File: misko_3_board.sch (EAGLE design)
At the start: 151 parts, among them CN1 LiPo Battery, IC1 MC1525TT, IC2 FT230XS, IC3 LTC4425, IC4 FM25W256-SOIC, Q1 FDN304P, U1 ATMEGA1281-16AU, U2 SN74HCT14DR, U3 SN74LVC1G3157DBVR - BT switch, U4 SN74LVC1G3157DBVR - GPS switch, U5 TMP36GRTZ-REEL7, U6 TPS63030DSKT, U7 MCP73871-2AAI/ML, X1 MINI-USB_4P-32005-101, X3 FH12-24S-0.5SH

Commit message: 3-deck board consisting of : deck 1: lower side: power supply, upper side: cpu, spi bus, deck 2: lower side: sim800 + holder, upper side: bluetooth module, gps supercap+circuit deck3: lower side: misc, upper side: oled connector, gps, buttons, usb connector, led connectors, power switch
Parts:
- removed BOTTOM, TOP: FH12-24S-0.5SH, con-hirose:FH12-24S-0.5SH
- removed C10: 10µF, resistor:C-EUC0805
- removed C12: 4.7µF, resistor:C-EUC0805
- removed L3: 1.5µH, inductor-neosid:MS50
- removed L5: DJNR6045-100-S, DJNR6045-100S Power Inductor:DJNR6045-100-S
- removed R22: 150k, rcl:R-EU_R0805
- removed S2: GPRS push, switch-omron:10-XX
- removed S3: right, switch-omron:10-XX
- removed S4: left, switch-omron:10-XX
- removed SUPERCAP: 1F, capacitor-wima:C5/2.5
- removed SV1: (no value), con-lstb:MA05-2
- removed SV2: (no value), con-lstb:MA04-1
- removed U6: TPS63030DSKT, Texas Instruments_By_element14_Batch_1:TPS63030DSKT
- added B10: bottom, con-lstb:MA10-1
- added BL20: bottom left, con-lsta:FE20-1
- added BR20: bottom right, con-lsta:FE20-1
- added BT, VCC, VCC1, VCC5, V_GPS, V_LIION: PTR1TP14R, testpad:PTR1TP14R
- added C41: 0.1µF, rcl:C-EUC0805
- added C42: 4.7µF, rcl:C-EUC0805
- added DOWN: down, switch-omron:10-XX
- added GPS, SIM800, TP2: PTR1B1,27, testpad:PTR1B1,27
- added JP2: I2C, jumper:JP1E
- added M10: mid, con-lstb:MA10-1
- added ML20: mid left, con-lsta:FE20-1
- added MR20: mid right, con-lsta:FE20-1
- added R58: 46k, resistor:R-EU_R0805
- added R59: 150k, resistor:R-EU_R0805
- added RIGHT: right, switch-omron:10-XX
- added T10: top, con-lstb:MA10-1
- added TL20: top left, con-lsta:FE20-1
- added TP6: TPPAD1-17Y, testpad:TPPAD1-17Y
- added TR20: top right, con-lsta:FE20-1
- added U$10: DJNR3015-1R5, DJNR3015-1R5 Inductor:DJNR3015-1R5
- added U$8: 1F, EECRG0V105 SuperCap:1F
- added U$9: TPS63001DRCR, TI TPS63031:TPS63001DRCR
- added UP: up, switch-omron:10-XX
- ANT2: value (none) -> U.FL-R-SMT 1
- BT_LED, GPRS_LED, GPS_GREEN_LED, GPS_RED_LED: device led:LEDSML1206 -> led:LEDSQR2X5
- C1, C15, C3, C30: device resistor:C-EUC1206 -> resistor:C-EUC0805
- C18: value 100nF -> 10µF; device resistor:C-EUC1206 -> rcl:C-EUC0805
- R1, R15, R36, R37, R38, R39, R4, R40, R41, R5, R50, R51, R6, R7: device resistor:R-EU_R1206 -> resistor:R-EU_R0805
- R14, R42, R43, R44, R52, R53, R57: device resistor:R-EU_R1206 -> rcl:R-EU_M0805
- R48: value 1k -> 46k; device resistor:R-EU_R1206 -> resistor:R-EU_R0805
- S1: value up -> left
- S6: value down -> GPRS
- SJ1: value (none) -> GPIO6
- SJ2: value (none) -> RESET
- USB_RX_LED, USB_TX_LED: device led:LEDSML1206 -> led:LEDCHIPLED_1206
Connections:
- net N$11 renamed VPCC
- net N$18 renamed THERM
- net N$22 renamed PROG1
- net N$23 renamed PROG3
- net N$24 renamed PFI
- net N$25 renamed LTC4425_PROG
- net N$26 renamed LTC4425_EN
- net N$27 renamed PFI_RET
- net N$32 renamed VMID
- net N$33 renamed GPIO7
- net N$36 renamed GPIO4
- net N$38 renamed GPIO6
- net N$40 renamed ADXL345SDA
- net N$46 renamed GSM_ANT
- net N$7 renamed USBDP
- net N$9 renamed USBDM
- net VBAT+ renamed V_LIION+
- removed net N$100: BOTTOM-23.1
- removed net N$12: IC2.RXD, R3.2
- removed net N$13: R1.2
- removed net N$15: U7.*TE, U7.CE, U7.PROG2, U7.SEL
- removed net N$3: IC2.TXD, R2.2
- removed net N$34: BT_LED.A, C6.2, Q1.D, U$3.VCC
- removed net N$44: GPRS_LED.A, R50.2
- removed net N$45: R50.1, U$1.NETLIGHT
- removed net N$47: U$1.GND10, U$1.GND9
- removed net N$48: U$1.GND6, U$1.GND7
- removed net N$5: L5.1, SV2.4
- removed net N$53: L3.2, U6.L1
- removed net N$54: L3.1, U6.L2
- removed net N$8: R5.1, USB_TX_LED.A
- removed net N$86: BOTTOM-21.1
- removed net N$87: BOTTOM-22.1
- removed net N$90: TOP-23.1
- removed net N$91: TOP-22.1
- removed net N$92: TOP-21.1
- removed net S1: C2.2, R8.2, U2.1A
- removed net S2: C4.2, R10.2, U2.2A
- removed net S3: C5.2, R12.2, U2.3A
- removed net S4: C7.2, R18.2, U2.4A
- removed net S5: C8.2, R17.2, U2.5A
- removed net S6: C9.2, R16.2, U2.6A
- removed net VBAT: C11.1, C12.2, C26.2, R51.2, S8.2, U$1.VBAT1, U$1.VBAT2, U$1.VRTC, U6.PS/SYNC, U6.VIN, U6.VINA, U7.OUT, U7.OUT_2
- new net BLUETOOTH: BR20.15, C8.2, MR20.15, R17.2, TR20.15, U2.5A
- new net BLUE_LED: BL20.14, BT_LED.A, C6.2, ML20.14, Q1.D, TL20.14, U$3.VCC
- new net DOWN: BR20.12, C4.2, MR20.12, R10.2, TR20.12, U2.2A
- new net EN: BL20.20, ML20.20, R59.2, S8.1, TL20.20, U$9.EN
- new net GPRS: BR20.16, C9.2, MR20.16, R16.2, TR20.16, U2.4A
- new net GPRS_LED: BR20.18, GPRS_LED.A, MR20.18, TR20.18, U$1.NETLIGHT
- new net GPS_ON_OFF: BL20.11, GPS.TP, ML20.11, R1.1, R36.1, TL20.11, TP2.TP, U$2.ON_OFF
- new net L1: U$10.L1, U$9.L1
- new net L2: U$10.L2, U$9.L2
- new net LEFT: BR20.11, C2.2, MR20.11, R8.2, TR20.11, U2.1A
- new net N$33: GPRS_LED.C, R50.1
- new net PA7: BL20.15, ML20.15, TL20.15, U1.PA7_(AD7)
- new net PD7: U1.(T0)_PD7
- new net PE2: B10.7, M10.7, T10.7, U1.(XCK0/AIN0)_PE2
- new net PE3: B10.6, M10.6, T10.6, U1.(OC3A/AIN1)_PE3
- new net PE7: U1.(ICP3/CLKO/INT7)_PE7
- new net PG0: U1.PG0_(~WR)
- new net PG1: U1.PG1_(~RD)
- new net PG2: BL20.16, ML20.16, TL20.16, U1.PG2_(ALE)
- new net RIGHT: BR20.14, C7.2, MR20.14, R18.2, TR20.14, U2.6A
- new net RXD: BL20.1, IC2.RXD, ML20.1, R3.2, TL20.1
- new net TXD: BL20.2, IC2.TXD, ML20.2, R2.2, TL20.2
- new net UP: BR20.13, C5.2, MR20.13, R12.2, TR20.13, U2.3A
- new net V_LIION_REGULATED: BL20.19, C11.1, C26.2, C42.2, ML20.19, R51.2, S8.2, TL20.19, U$1.VBAT1, U$1.VBAT2, U$1.VRTC, U$9.PS/SYNC, U$9.VIN, U$9.VINA, U7.OUT, U7.OUT_2, V_LIION.TP
- new net V_SUPERCAP_SENSE_PIN: R48.2, R58.1, U1.PF2_(ADC2)
- net 5V0: now also BR20.20, MR20.20, TR20.20, U7.*TE, U7.CE, U7.PROG2, U7.SEL; no longer C18.2, L5.2
- net ADXL345_INT1_INTERRUPT_PIN: now also U1.(T3/INT6)_PE6; no longer U1.(ICP3/CLKO/INT7)_PE7
- net ANALOG_SW_CTRL_PIN: now also BR20.1, MR20.1, TR20.1, U1.(OC1B/PCINT6)_PB6, VCC1.TP; no longer BOTTOM-13.1, TOP-13.1, U1.(TOSC2)_PG3
- net ANTENNA: now also ANT2.ANT; no longer ANT2.1
- net BAT_A_PIN: now also U1.PF3_(ADC3); no longer U1.PF2_(ADC2)
- net BLUETOOTH_WAKEUP_PIN: now also BL20.13, BT.TP, ML20.13, TL20.13, U1.PA3_(AD3); no longer U1.(OC0A/OC1C/PCINT7)_PB7
- net GND: now also ANT2.GND1, ANT2.GND2, B10.9, BL20.5, BR20.5, C41.2, C42.1, DOWN.P, DOWN.P1, M10.9, ML20.5, MR20.5, R50.2, R58.2, R59.1, RIGHT.P, RIGHT.P1, T10.9, TL20.5, TP6.TP, TR20.5, U$1.GND10, U$1.GND6, U$1.GND7, U$1.GND9, U$7.GND6, U$7.GND7, U$8.+, U$9.GND, U$9.PGND, UP.P, UP.P1; no longer BOTTOM-1.1, BOTTOM-24.1, C10.1, C12.1, GPRS_LED.C, R22.2, S2.P, S2.P1, S3.P, S3.P1, S4.P, S4.P1, SUPERCAP.1, SV1.10, SV1.2, SV2.1, TOP-1.1, TOP-24.1, U6.GND, U6.PGND
- net GPS_GREEN_LED_PIN: now also BL20.17, ML20.17, TL20.17; no longer BOTTOM-10.1, BOTTOM-12.1, TOP-10.1, TOP-12.1
- net GPS_POWER_CTL_PIN: now also R1.2, U1.PA2_(AD2); no longer BOTTOM-18.1, R1.1, R36.1, TOP-18.1, U$2.ON_OFF, U1.(T0)_PD7
- net GPS_RED_LED_PIN: now also BL20.18, ML20.18, TL20.18; no longer BOTTOM-11.1, BOTTOM-9.1, TOP-11.1, TOP-9.1
- net GPS_SW_SERIAL_RX: now also B10.2, M10.2, T10.2; no longer BOTTOM-19.1, TOP-19.1
- net GPS_SW_SERIAL_TX: now also B10.1, M10.1, T10.1; no longer BOTTOM-20.1, TOP-20.1
- net GPS_TX: now also BL20.12, ML20.12, TL20.12
- net GPS_WAKEUP_PIN: now also BL20.10, ML20.10, TL20.10, U1.PA1_(AD1); no longer BOTTOM-17.1, TOP-17.1, U1.(TOSC1)_PG4
- net I2C_SCL_PIN: now also JP2.1; no longer SV2.3
- net I2C_SDA_PIN: now also JP2.2; no longer SV2.2
- net JTAG_TCL_PIN: now also BL20.6, ML20.6, TL20.6; no longer SV1.1
- net JTAG_TDI_PIN: now also BL20.9, ML20.9, TL20.9; no longer SV1.9
- net JTAG_TDO_PIN: now also BL20.8, ML20.8, TL20.8; no longer SV1.3
- net JTAG_TMS_PIN: now also BL20.7, ML20.7, TL20.7; no longer SV1.5
- net MCP73871_CHARGE_STATUS_1_PIN: now also U1.PA4_(AD4); no longer U1.PA2_(AD2)
- net MCP73871_CHARGE_STATUS_2_PIN: now also U1.PA5_(AD5); no longer U1.PA1_(AD1)
- net MCP73871_POWER_GOOD_PIN: now also U1.PA6_(AD6); no longer U1.PA0_(AD0)
- net MENU_BLUETOOTH_POWER_TOGGLE_PIN: now also U1.PC4_(A12); no longer BOTTOM-4.1, TOP-4.1, U1.PC1_(A9)
- net MENU_DOWN_BUTTON_PIN: now also U1.PC1_(A9), U2.2Y; no longer BOTTOM-5.1, TOP-5.1, U1.PC2_(A10), U2.6Y
- net MENU_GPRS_PUSH_BUTTON_PIN: now also U1.PC5_(A13), U2.4Y; no longer BOTTOM-7.1, TOP-7.1, U1.PC4_(A12), U2.2Y
- net MENU_LEFT_BUTTON_PIN: now also U2.1Y; no longer BOTTOM-3.1, TOP-3.1, U2.4Y
- net MENU_RIGHT_BUTTON_PIN: now also U1.PC3_(A11), U2.6Y; no longer BOTTOM-8.1, TOP-8.1, U1.PC5_(A13), U2.3Y
- net MENU_UP_BUTTON_PIN: now also U1.PC2_(A10), U2.3Y; no longer BOTTOM-6.1, TOP-6.1, U1.PC3_(A11), U2.1Y
- net N$1: now also R5.2, USB_TX_LED.A; no longer R22.1, S8.1, U6.EN
- net N$16: now also UP.S, UP.S1; no longer S3.S, S3.S1
- net N$21: now also DOWN.S, DOWN.S1; no longer S2.S, S2.S1
- net N$30: now also RIGHT.S, RIGHT.S1; no longer S4.S, S4.S1
- net PDI_UART0_CTS_PIN: now also BL20.3, ML20.3, TL20.3; no longer BOTTOM-16.1, TOP-16.1
- net PDI_UART0_RX_PIN: no longer BOTTOM-14.1, TOP-14.1
- net PDI_UART0_TX_PIN: no longer BOTTOM-15.1, TOP-15.1
- net RESET: now also BR20.17, MR20.17, TR20.17; no longer SV1.6
- net SD_CARD_DETECT_PIN: no longer U1.(OC1B/PCINT6)_PB6
- net SIM800C_CTS_PIN: now also BR20.8, MR20.8, TR20.8
- net SIM800C_POWER_PIN: now also BR20.10, MR20.10, SIM800.TP, TR20.10; no longer R48.1, U$1.VDD_EXT
- net SIM800C_RX_PIN: now also BR20.6, MR20.6, TR20.6
- net SIM800C_STATUS_PIN: now also BR20.9, MR20.9, TR20.9
- net SIM800C_TX_PIN: now also BR20.7, MR20.7, TR20.7
- net SIM_DETECT: no longer R48.2
- net SPI_FRAM_SS_PIN: now also U1.(OC3B/INT4)_PE4; no longer U1.(~SS/PCINT0)_PB0
- net SPI_MISO_PIN: now also B10.3, M10.3, T10.3
- net SPI_MOSI_PIN: now also B10.4, M10.4, T10.4
- net SPI_OLED_D/C_PIN: now also BR20.3, MR20.3, TR20.3, U1.(TOSC2)_PG3; no longer U1.(OC3B/INT4)_PE4
- net SPI_OLED_RESET_PIN: now also BR20.2, MR20.2, TR20.2, U1.(OC0A/OC1C/PCINT7)_PB7; no longer U1.(OC3A/AIN1)_PE3
- net SPI_SCK_PIN: now also B10.5, M10.5, T10.5
- net SPI_SS_ADXL345_PIN: now also U1.(OC3C/INT5)_PE5; no longer U1.(XCK0/AIN0)_PE2
- net SPI_SS_OLED_PIN: now also BR20.4, MR20.4, TR20.4, U1.(TOSC1)_PG4; no longer U1.(OC3C/INT5)_PE5
- net SPI_SS_SD_CARD_PIN: now also U1.(~SS/PCINT0)_PB0; no longer U1.(T3/INT6)_PE6
- net TMP36_SHUTDOWN_PIN: now also U1.PA0_(AD0); no longer U1.PA3_(AD3)
- net VCC: now also BL20.4, BR20.19, C18.2, C41.1, ML20.4, MR20.19, TL20.4, TR20.19, U$7.VCC, U$9.FB, U$9.VOUT, VCC.TP, VCC5.TP; no longer BOTTOM-2.1, C10.2, SV1.4, TOP-2.1, U6.FB, U6.VOUT
- net VGPS: now also B10.8, M10.8, R48.1, T10.8, U$8.-, V_GPS.TP; no longer SUPERCAP.2
- net VUSB: now also R5.1; no longer R5.2
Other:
- note added: "VUSB (aka. supercap voltage) measurement"
- note removed: "I2C Connector"
- note removed: "JTAG Header"
- moved on the sheet: BT_LED, C18, C28, C29, GPRS_LED, GPS_GREEN_LED, GPS_RED_LED, L2, R36, R4, R41, R45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

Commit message: - further progress on the 3-deck board, top portion needs rework due to final oled module
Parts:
- removed C30: 100nF, resistor:C-EUC0805
- removed DOWN: down, switch-omron:10-XX
- removed L1: DJNR6045-100-S, DJNR6045-100S Power Inductor:DJNR6045-100-S
- removed RIGHT: right, switch-omron:10-XX
- removed S1: left, switch-omron:10-XX
- removed S5: Bluetooth, switch-omron:10-XX
- removed S6: GPRS, switch-omron:10-XX
- removed UP: up, switch-omron:10-XX
- removed X1: MINI-USB_4P-32005-101, con-cypressindustries:MINI-USB_4P-32005-101
- added BLUETOOTH: BT, switch-omron:10-XX
- added C10: 100nF, resistor:C-EUC0805
- added GPRS: gprs, switch-omron:10-XX
- added L3: DJNR6045-100-S, DJNR6045-100S Power Inductor:DJNR6045-100-S
- added U$11: MX500075-1517USB_MINI-B, MX500075-1517 USB Mini-B straight socket:MX500075-1517USB_MINI-B
- added U$12: MICROJOYSTICK, micro joystick:MICROJOYSTICK
- U$8: value 1F -> EECS5R5H155; device EECRG0V105 SuperCap:1F -> EECS5R5H155 Supercap:EECS5R5H155
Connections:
- removed net N$14: R8.1, R9.1, S1.S, S1.S1
- removed net N$16: R12.1, R13.1, UP.S, UP.S1
- removed net N$21: DOWN.S, DOWN.S1, R10.1, R11.1
- removed net N$28: R17.1, R20.1, S5.S, S5.S1
- removed net N$29: R16.1, R19.1, S6.S, S6.S1
- removed net N$30: R18.1, R21.1, RIGHT.S, RIGHT.S1
- new net BUTTON_BLUETOOTH: BLUETOOTH.S, BLUETOOTH.S1, R17.1, R20.1
- new net BUTTON_CENTER: U$12.CENTER
- new net BUTTON_DOWN: R10.1, R11.1, U$12.DOWN
- new net BUTTON_GPRS: GPRS.S, GPRS.S1, R16.1, R19.1
- new net BUTTON_LEFT: R8.1, R9.1, U$12.LEFT
- new net BUTTON_RIGHT: R18.1, R21.1, U$12.RIGHT
- new net BUTTON_UP: R12.1, R13.1, U$12.UP
- net 5V0: now also C10.2, L3.2; no longer C30.2, L1.1
- net GND: now also BLUETOOTH.P, BLUETOOTH.P1, C10.1, GPRS.P, GPRS.P1, U$11.GND, U$12.GND1; no longer C30.1, DOWN.P, DOWN.P1, RIGHT.P, RIGHT.P1, S1.P, S1.P1, S5.P, S5.P1, S6.P, S6.P1, UP.P, UP.P1, X1.4
- net USB_D+: now also U$11.DP; no longer X1.3
- net USB_D-: now also U$11.DN; no longer X1.2
- net VUSB: now also L3.1, U$11.VBUS; no longer L1.2, X1.1

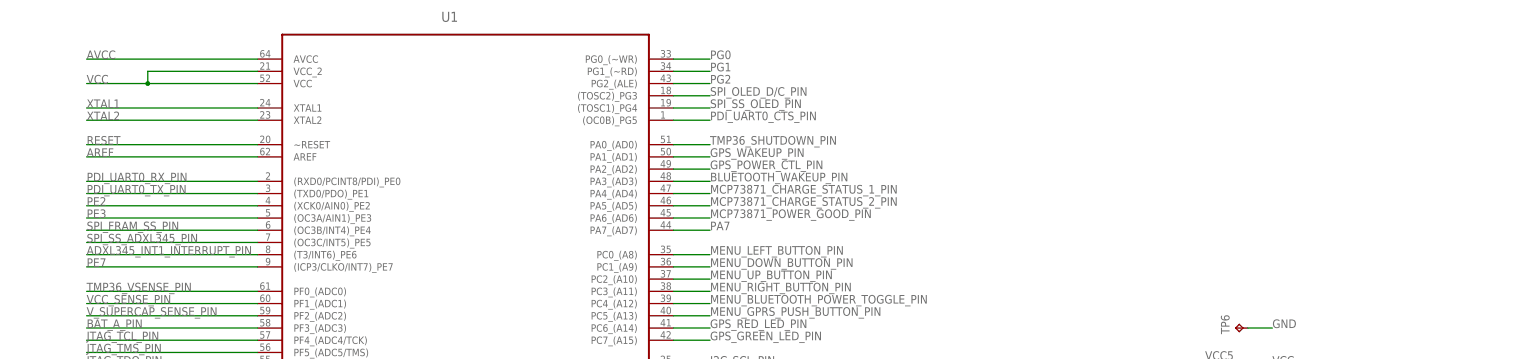
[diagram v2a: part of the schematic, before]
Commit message: - correction of int7 pin (-> adxl345 int1)
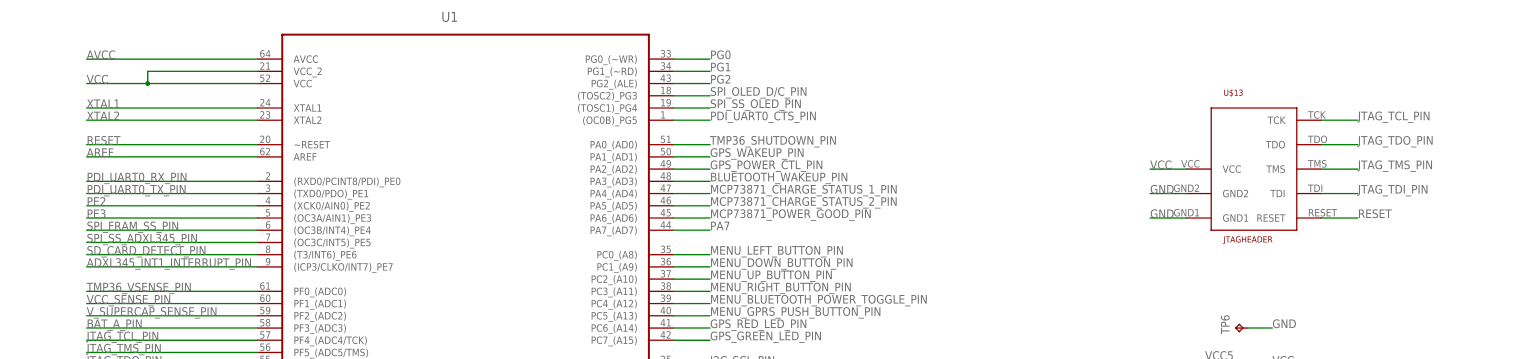
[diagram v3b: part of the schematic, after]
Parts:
- added U$13: JTAGHEADER, DS1031-14 - IDC socket:JTAGHEADER
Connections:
- removed net PE7: U1.(ICP3/CLKO/INT7)_PE7
- net ADXL345_INT1_INTERRUPT_PIN: now also U1.(ICP3/CLKO/INT7)_PE7; no longer U1.(T3/INT6)_PE6
- net GND: now also U$13.GND1, U$13.GND2
- net JTAG_TCL_PIN: now also U$13.TCK
- net JTAG_TDI_PIN: now also U$13.TDI
- net JTAG_TDO_PIN: now also U$13.TDO
- net JTAG_TMS_PIN: now also U$13.TMS
- net RESET: now also U$13.RESET
- net SD_CARD_DETECT_PIN: now also U1.(T3/INT6)_PE6
- net VCC: now also U$13.VCC
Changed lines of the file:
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@@
 <part name="BLUETOOTH" library="switch-omron" deviceset="10-XX" device="" value="BT"/>
 <part name="GPRS" library="switch-omron" deviceset="10-XX" device="" value="gprs"/>
+<part name="U$13" library="DS1031-14 - IDC socket" deviceset="JTAGHEADER" device=""/>
 </parts>
 <sheets>
@@
 <instance part="BLUETOOTH" gate="1" x="20.32" y="388.62" rot="R270"/>
 <instance part="GPRS" gate="1" x="20.32" y="363.22" rot="R270"/>
+<instance part="U$13" gate="G$1" x="294.64" y="802.64"/>
 </instances>
 <busses>
@@
 <label x="279.4" y="759.46" size="1.778" layer="95"/>
 </segment>
+<segment>
+<pinref part="U$13" gate="G$1" pin="VCC"/>
+<wire x1="261.62" y1="800.1" x2="254" y2="800.1" width="0.1524" layer="91"/>
+<label x="254" y="800.1" size="1.778" layer="95"/>
+</segment>
 </net>
 <net name="GND" class="0">
@@
 <label x="208.28" y="342.9" size="1.778" layer="95"/>
 </segment>
+<segment>
+<pinref part="U$13" gate="G$1" pin="GND1"/>
+<wire x1="261.62" y1="789.94" x2="254" y2="789.94" width="0.1524" layer="91"/>
+<label x="254" y="789.94" size="1.778" layer="95"/>
+</segment>
+<segment>
+<pinref part="U$13" gate="G$1" pin="GND2"/>
+<wire x1="261.62" y1="795.02" x2="254" y2="795.02" width="0.1524" layer="91"/>
+<label x="254" y="795.02" size="1.778" layer="95"/>
+</segment>
 </net>
 <net name="5V0" class="1">
@@
 <label x="523.24" y="782.32" size="1.778" layer="95"/>
 </segment>
+<segment>
+<pinref part="U$13" gate="G$1" pin="TDI"/>
+<wire x1="289.56" y1="795.02" x2="297.18" y2="795.02" width="0.1524" layer="91"/>
+<label x="297.18" y="795.02" size="1.778" layer="95"/>
+</segment>
 </net>
 <net name="JTAG_TDO_PIN" class="2">
@@
 <label x="523.24" y="779.78" size="1.778" layer="95"/>
 </segment>
+<segment>
+<pinref part="U$13" gate="G$1" pin="TDO"/>
+<wire x1="289.56" y1="805.18" x2="297.18" y2="805.18" width="0.1524" layer="91"/>
+<label x="297.18" y="805.18" size="1.778" layer="95"/>
+</segment>
 </net>
 <net name="JTAG_TMS_PIN" class="2">
@@
 <label x="523.24" y="777.24" size="1.778" layer="95"/>
 </segment>
+<segment>
+<pinref part="U$13" gate="G$1" pin="TMS"/>
+<wire x1="289.56" y1="800.1" x2="297.18" y2="800.1" width="0.1524" layer="91"/>
+<label x="297.18" y="800.1" size="1.778" layer="95"/>
+</segment>
 </net>
 <net name="JTAG_TCL_PIN" class="2">
@@
 <label x="523.24" y="774.7" size="1.778" layer="95"/>
 </segment>
+<segment>
+<pinref part="U$13" gate="G$1" pin="TCK"/>
+<wire x1="289.56" y1="810.26" x2="297.18" y2="810.26" width="0.1524" layer="91"/>
+<label x="297.18" y="810.26" size="1.778" layer="95"/>
+</segment>
 </net>
 <net name="BAT_A_PIN" class="2">
@@
 </segment>
 <segment>
-<pinref part="U1" gate="A" pin="(T3/INT6)_PE6"/>
-<wire x1="68.58" y1="782.32" x2="33.02" y2="782.32" width="0.1524" layer="91"/>
-<label x="33.02" y="782.32" size="1.778" layer="95"/>
+<pinref part="U1" gate="A" pin="(ICP3/CLKO/INT7)_PE7"/>
+<wire x1="68.58" y1="779.78" x2="33.02" y2="779.78" width="0.1524" layer="91"/>
+<label x="33.02" y="779.78" size="1.778" layer="95"/>
 </segment>
 </net>
@@
 <label x="317.5" y="-149.86" size="1.778" layer="95"/>
 </segment>
+<segment>
+<pinref part="U1" gate="A" pin="(T3/INT6)_PE6"/>
+<wire x1="68.58" y1="782.32" x2="33.02" y2="782.32" width="0.1524" layer="91"/>
+<label x="33.02" y="782.32" size="1.778" layer="95"/>
+</segment>
 </net>
 <net name="BLUETOOTH_WAKEUP_PIN" class="2">
@@
 <label x="523.24" y="726.44" size="1.778" layer="95"/>
 </segment>
+<segment>
+<pinref part="U$13" gate="G$1" pin="RESET"/>
+<wire x1="289.56" y1="789.94" x2="297.18" y2="789.94" width="0.1524" layer="91"/>
+<label x="297.18" y="789.94" size="1.778" layer="95"/>
+</segment>
 </net>
 <net name="XTAL2" class="0">
@@
 </segment>
 </net>
-<net name="PE7" class="0">
-<segment>
-<pinref part="U1" gate="A" pin="(ICP3/CLKO/INT7)_PE7"/>
-<wire x1="68.58" y1="779.78" x2="33.02" y2="779.78" width="0.1524" layer="91"/>
-<label x="33.02" y="779.78" size="1.778" layer="95"/>
-</segment>
-</net>
